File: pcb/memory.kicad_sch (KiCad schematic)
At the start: 0 parts

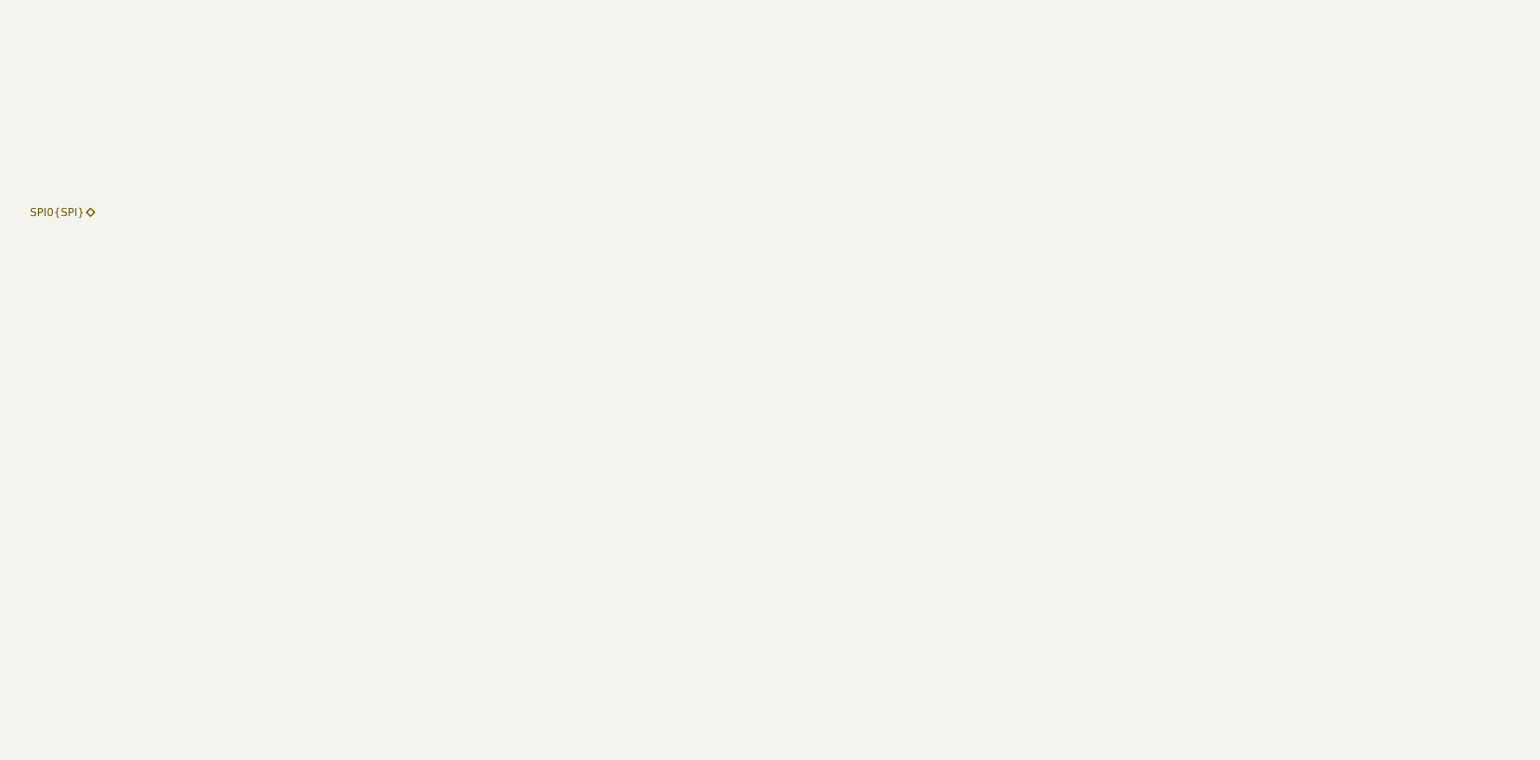
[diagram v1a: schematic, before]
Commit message: current sense hierarchy definition
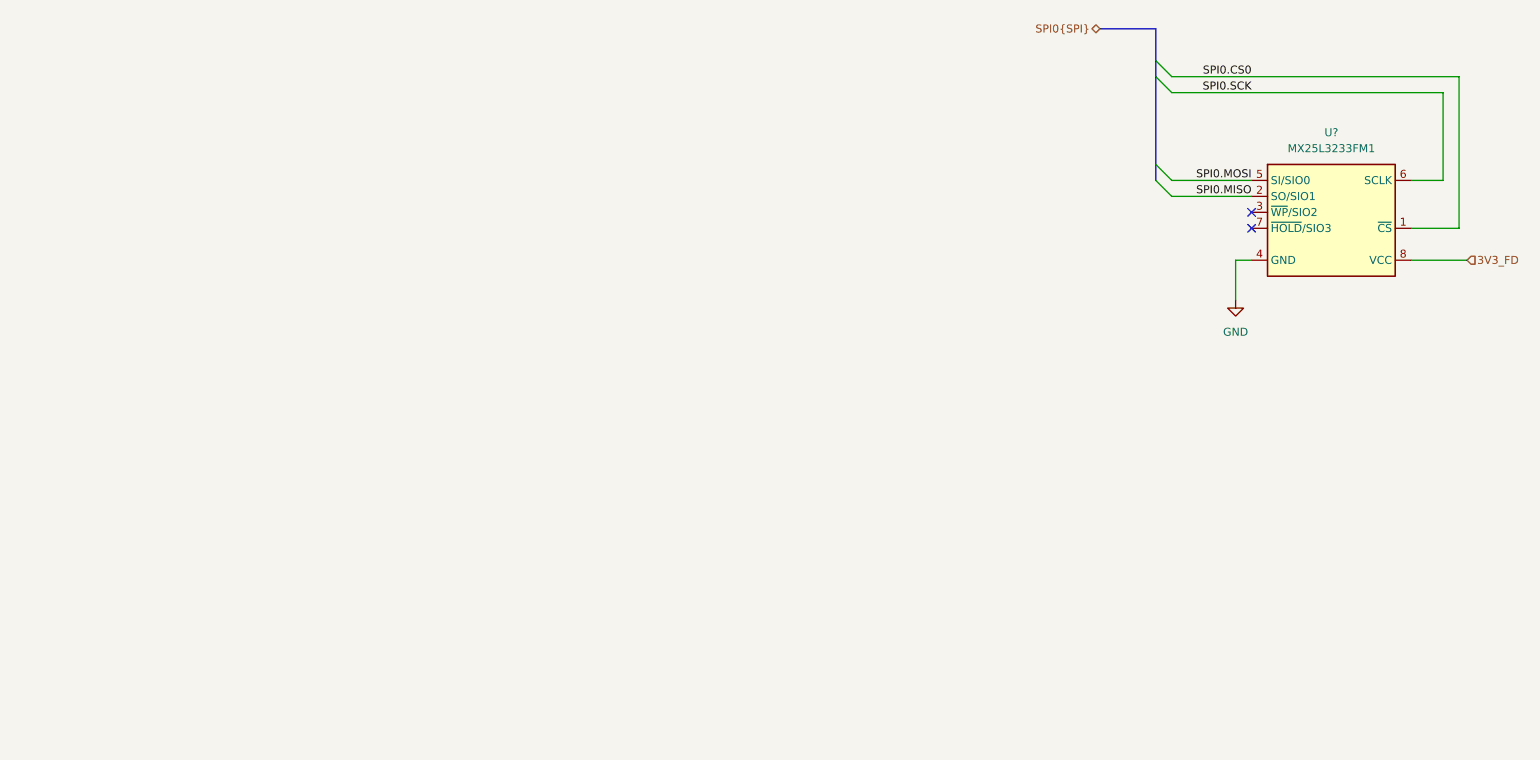
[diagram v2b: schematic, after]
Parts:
- added U?: MX25L3233FM1, Package_SO:JEITA_SOIC-8_3.9x4.9mm_P1.27mm, symbol Memory_Flash:MX25L3233FM1
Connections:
- new net 3V3_FD: U?.8 (VCC)
- new net GND: U?.4 (GND)
- new net SPI0.CS0: U?.1 (~{CS})
- new net SPI0.MISO: U?.2 (SO/SIO1)
- new net SPI0.MOSI: U?.5 (SI/SIO0)
- new net SPI0.SCK: U?.6 (SCLK)
- no-connect marks 0 -> 2

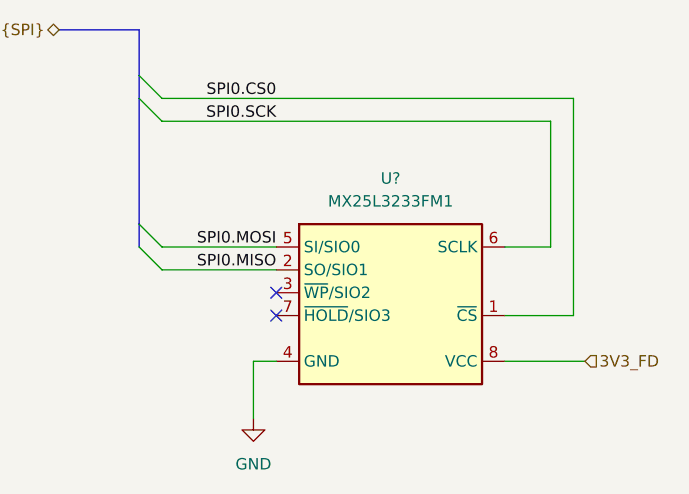
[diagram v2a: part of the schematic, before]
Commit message: changed spi flash to wson
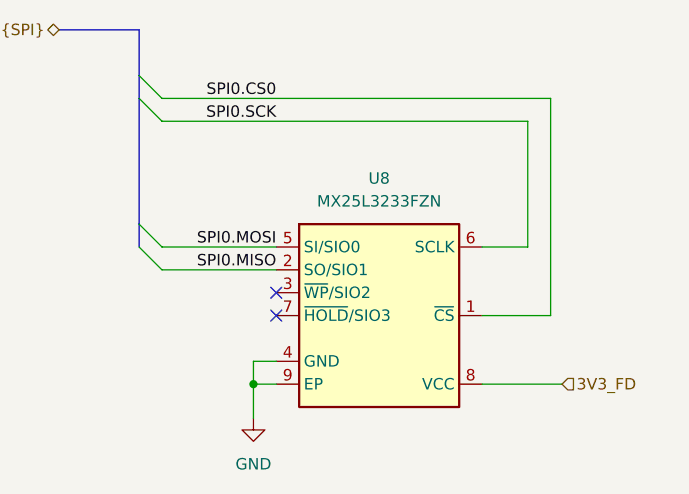
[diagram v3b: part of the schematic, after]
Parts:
- removed U?: MX25L3233FM1, Package_SO:JEITA_SOIC-8_3.9x4.9mm_P1.27mm, symbol Memory_Flash:MX25L3233FM1
- added U8: MX25L3233FZN, Package_SON:WSON-8-1EP_6x5mm_P1.27mm_EP3.4x4mm, symbol Memory_Flash:MX25L3233FZN
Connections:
- net 3V3_FD: now also U8.8 (VCC)
- net GND: now also U8.4 (GND), U8.9 (EP)
- net SPI0.CS0: now also U8.1 (~{CS})
- net SPI0.MISO: now also U8.2 (SO/SIO1)
- net SPI0.MOSI: now also U8.5 (SI/SIO0)
- net SPI0.SCK: now also U8.6 (SCLK)
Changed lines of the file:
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@@
 		(company "Andre S Winkel")
+	)
+	(junction
+		(at 234.95 66.04)
+		(diameter 0)
+		(color 0 0 0 0)
 	)
 	(no_connect
@@
 	(wire
 		(pts
-			(xy 262.89 50.8) (xy 267.97 50.8)
+			(xy 260.35 50.8) (xy 265.43 50.8)
 		)
 		(stroke
@@
 	(wire
 		(pts
-			(xy 270.51 34.29) (xy 270.51 58.42)
+			(xy 267.97 34.29) (xy 267.97 58.42)
 		)
 		(stroke
@@
 	(wire
 		(pts
-			(xy 267.97 36.83) (xy 267.97 50.8)
-		)
-		(stroke
-			(width 0)
-			(type default)
-		)
-	)
-	(wire
-		(pts
-			(xy 262.89 63.5) (xy 271.78 63.5)
-		)
-		(stroke
-			(width 0)
-			(type default)
-		)
-	)
-	(wire
-		(pts
-			(xy 224.79 36.83) (xy 267.97 36.83)
-		)
-		(stroke
-			(width 0)
-			(type default)
-		)
-	)
-	(wire
-		(pts
-			(xy 234.95 63.5) (xy 234.95 69.85)
-		)
-		(stroke
-			(width 0)
-			(type default)
-		)
-	)
-	(wire
-		(pts
-			(xy 262.89 58.42) (xy 270.51 58.42)
+			(xy 265.43 36.83) (xy 265.43 50.8)
+		)
+		(stroke
+			(width 0)
+			(type default)
+		)
+	)
+	(wire
+		(pts
+			(xy 260.35 66.04) (xy 269.24 66.04)
+		)
+		(stroke
+			(width 0)
+			(type default)
+		)
+	)
+	(wire
+		(pts
+			(xy 234.95 66.04) (xy 237.49 66.04)
+		)
+		(stroke
+			(width 0)
+			(type default)
+		)
+	)
+	(wire
+		(pts
+			(xy 224.79 36.83) (xy 265.43 36.83)
+		)
+		(stroke
+			(width 0)
+			(type default)
+		)
+	)
+	(wire
+		(pts
+			(xy 234.95 63.5) (xy 234.95 66.04)
+		)
+		(stroke
+			(width 0)
+			(type default)
+		)
+	)
+	(wire
+		(pts
+			(xy 260.35 58.42) (xy 267.97 58.42)
 		)
 		(stroke
@@
 	(wire
 		(pts
-			(xy 224.79 34.29) (xy 270.51 34.29)
+			(xy 234.95 66.04) (xy 234.95 69.85)
+		)
+		(stroke
+			(width 0)
+			(type default)
+		)
+	)
+	(wire
+		(pts
+			(xy 224.79 34.29) (xy 267.97 34.29)
 		)
 		(stroke
@@
 	(hierarchical_label "3V3_FD"
 		(shape input)
-		(at 271.78 63.5 0)
+		(at 269.24 66.04 0)
 		(effects
 			(font
@@
 	)
 	(symbol
-		(lib_id "Memory_Flash:MX25L3233FM1")
-		(at 250.19 57.15 0)
+		(lib_id "Memory_Flash:MX25L3233FZN")
+		(at 248.92 58.42 0)
 		(unit 1)
 		(exclude_from_sim no)
@@
 		(on_board yes)
 		(dnp no)
-		(property "Reference" "U?"
-			(at 250.19 43.18 0)
-			(effects
-				(font
-					(size 1.27 1.27)
-				)
-			)
-		)
-		(property "Value" "MX25L3233FM1"
-			(at 250.19 45.72 0)
-			(effects
-				(font
-					(size 1.27 1.27)
-				)
-			)
-		)
-		(property "Footprint" "Package_SO:JEITA_SOIC-8_3.9x4.9mm_P1.27mm"
-			(at 250.19 72.39 0)
+		(fields_autoplaced yes)
+		(property "Reference" "U8"
+			(at 248.92 43.18 0)
+			(effects
+				(font
+					(size 1.27 1.27)
+				)
+			)
+		)
+		(property "Value" "MX25L3233FZN"
+			(at 248.92 45.72 0)
+			(effects
+				(font
+					(size 1.27 1.27)
+				)
+			)
+		)
+		(property "Footprint" "Package_SON:WSON-8-1EP_6x5mm_P1.27mm_EP3.4x4mm"
+			(at 248.92 73.66 0)
 			(effects
 				(font
@@
 		)
 		(property "Datasheet" "https://www.macronix.com/Lists/Datasheet/Attachments/8377/MX25L3233F,%203V,%2032Mb,%20v1.1.pdf"
-			(at 250.19 74.676 0)
+			(at 248.92 75.946 0)
 			(effects
 				(font
@@
 			)
 		)
-		(property "Description" "32-Mbit, 3V (2.65V-3.6V) SPI Serial Flash Memory, JEITA SOIC-8 (SOP-8)"
-			(at 247.65 69.85 0)
+		(property "Description" "32-Mbit, 3V (2.65V-3.6V) SPI Serial Flash Memory, WSON-8"
+			(at 247.65 58.42 0)
 			(effects
 				(font
@@
 		)
 		(property "Name" ""
-			(at 250.19 57.15 0)
+			(at 248.92 58.42 0)
 			(effects
 				(font
@@
 			)
 		)
+		(pin "4"
+		)
+		(pin "8"
+		)
+		(pin "7"
+		)
+		(pin "3"
+		)
+		(pin "2"
+		)
+		(pin "5"
+		)
+		(pin "6"
+		)
 		(pin "1"
 		)
-		(pin "6"
-		)
-		(pin "5"
-		)
-		(pin "2"
-		)
-		(pin "3"
-		)
-		(pin "7"
-		)
-		(pin "8"
-		)
-		(pin "4"
+		(pin "9"
 		)
 		(instances
 			(project ""
 				(path "/e63e39d7-6ac0-4ffd-8aa3-1841a4541b55/59d21473-a004-4514-8090-fd93db818925/b633a666-4c3d-4ac9-9e0f-b350177ade0b"
-					(reference "U?")
+					(reference "U8")
 					(unit 1)
 				)

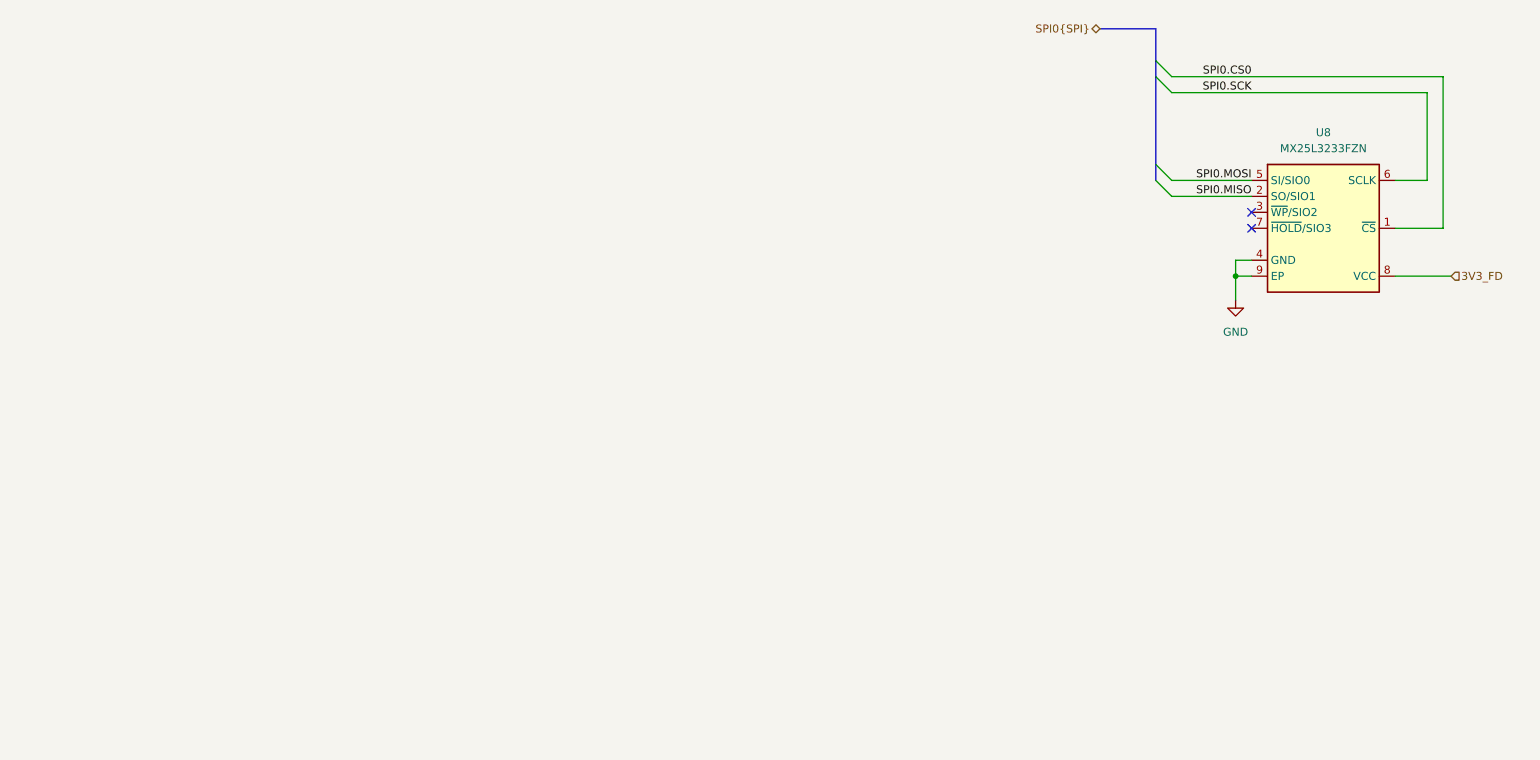
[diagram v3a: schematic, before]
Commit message: added dram, defined pcie sideband sigs.
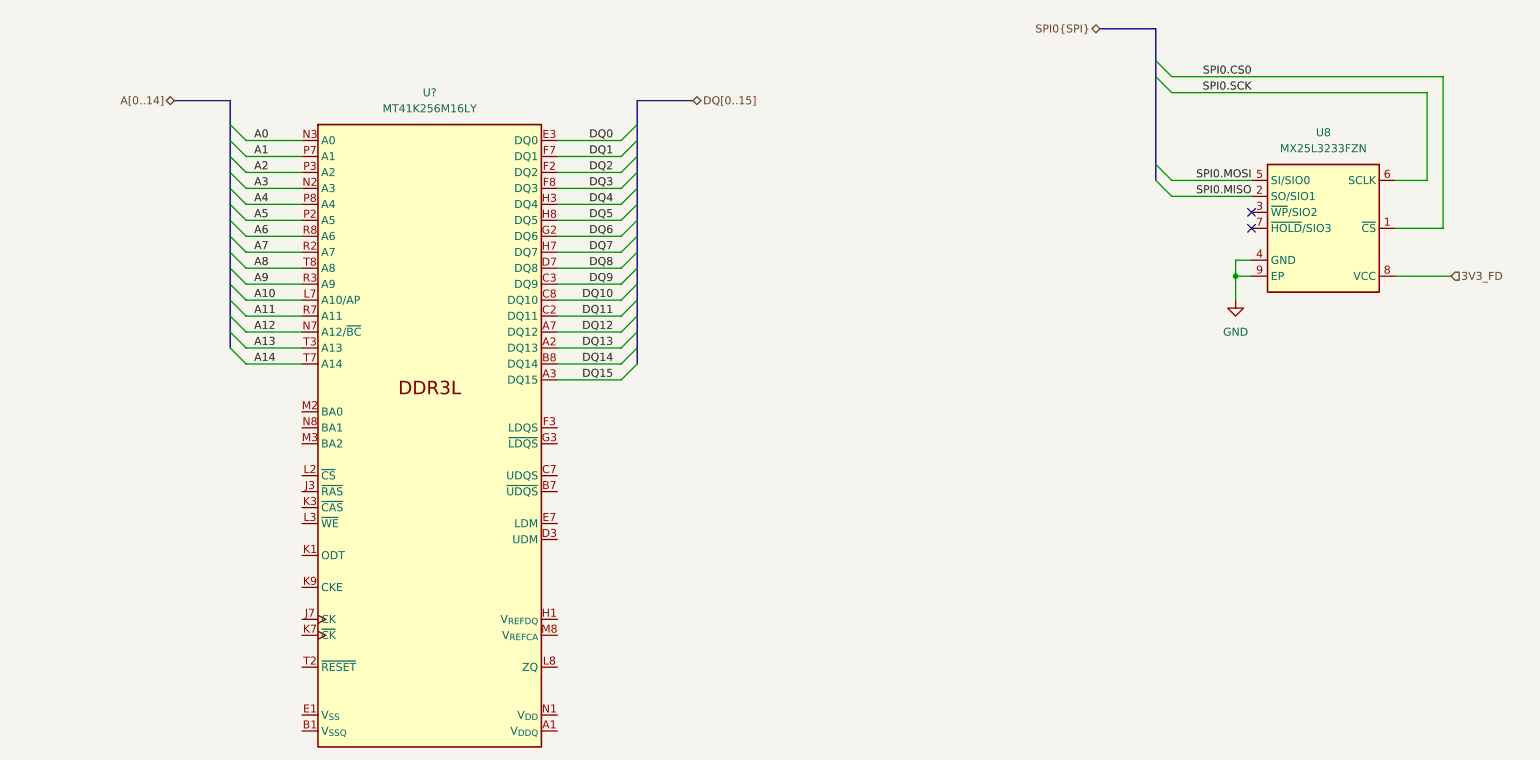
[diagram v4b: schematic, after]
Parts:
- added U?: MT41K256M16LY, Package_BGA:Micron_FBGA-96_7.5x13.5mm_Layout9x16_P0.8mm, symbol Memory_RAM:MT41K256M16LY
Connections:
- new net: U?.A8 (V_{DDQ}), U?.C1 (V_{DDQ}), U?.C9 (V_{DDQ}), U?.D2 (V_{DDQ}), U?.E9 (V_{DDQ}), U?.F1 (V_{DDQ}), U?.H2 (V_{DDQ}), U?.H9 (V_{DDQ})
- new net: U?.A9 (V_{SS}), U?.B3 (V_{SS}), U?.G8 (V_{SS}), U?.J2 (V_{SS}), U?.J8 (V_{SS}), U?.M1 (V_{SS}), U?.M9 (V_{SS}), U?.P1 (V_{SS}), U?.P9 (V_{SS}), U?.T1 (V_{SS}), U?.T9 (V_{SS})
- new net: U?.B2 (V_{DD}), U?.D9 (V_{DD}), U?.G7 (V_{DD}), U?.K2 (V_{DD}), U?.K8 (V_{DD}), U?.N9 (V_{DD}), U?.R1 (V_{DD}), U?.R9 (V_{DD})
- new net: U?.B9 (V_{SSQ}), U?.D1 (V_{SSQ}), U?.D8 (V_{SSQ}), U?.E2 (V_{SSQ}), U?.E8 (V_{SSQ}), U?.F9 (V_{SSQ}), U?.G1 (V_{SSQ}), U?.G9 (V_{SSQ})
- new net A0: U?.N3 (A0)
- new net A1: U?.P7 (A1)
- new net A10: U?.L7 (A10/AP)
- new net A11: U?.R7 (A11)
- new net A12: U?.N7 (A12/~{BC})
- new net A13: U?.T3 (A13)
- new net A14: U?.T7 (A14)
- new net A2: U?.P3 (A2)
- new net A3: U?.N2 (A3)
- new net A4: U?.P8 (A4)
- new net A5: U?.P2 (A5)
- new net A6: U?.R8 (A6)
- new net A7: U?.R2 (A7)
- new net A8: U?.T8 (A8)
- new net A9: U?.R3 (A9)
- new net DQ0: U?.E3 (DQ0)
- new net DQ1: U?.F7 (DQ1)
- new net DQ10: U?.C8 (DQ10)
- new net DQ11: U?.C2 (DQ11)
- new net DQ12: U?.A7 (DQ12)
- new net DQ13: U?.A2 (DQ13)
- new net DQ14: U?.B8 (DQ14)
- new net DQ15: U?.A3 (DQ15)
- new net DQ2: U?.F2 (DQ2)
- new net DQ3: U?.F8 (DQ3)
- new net DQ4: U?.H3 (DQ4)
- new net DQ5: U?.H8 (DQ5)
- new net DQ6: U?.G2 (DQ6)
- new net DQ7: U?.H7 (DQ7)
- new net DQ8: U?.D7 (DQ8)
- new net DQ9: U?.C3 (DQ9)

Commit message: ddr3
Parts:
- added U?: TCR2EE135, Package_TO_SOT_SMD:SOT-553, symbol Regulator_Linear:TCR2EE135
- gave numbers to parts that had none: 1
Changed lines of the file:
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@@
+	)
+	(symbol
+		(lib_id "Regulator_Linear:TCR2EE135")
+		(at 165.1 100.33 0)
+		(unit 1)
+		(exclude_from_sim no)
+		(in_bom yes)
+		(on_board yes)
+		(dnp no)
+		(fields_autoplaced yes)
+		(property "Reference" "U?"
+			(at 165.1 90.17 0)
+			(effects
+				(font
+					(size 1.27 1.27)
+				)
+			)
+		)
+		(property "Value" "TCR2EE135"
+			(at 165.1 92.71 0)
+			(effects
+				(font
+					(size 1.27 1.27)
+				)
+			)
+		)
+		(property "Footprint" "Package_TO_SOT_SMD:SOT-553"
+			(at 165.1 110.49 0)
+			(effects
+				(font
+					(size 1.27 1.27)
+				)
+				(hide yes)
+			)
+		)
+		(property "Datasheet" "https://toshiba.semicon-storage.com/info/docget.jsp?did=13794&prodName=TCR2EF45"
+			(at 158.75 93.98 0)
+			(effects
+				(font
+					(size 1.27 1.27)
+				)
+				(hide yes)
+			)
+		)
+		(property "Description" "200mA Low-dropout Voltage Regulator, Vout 1.35V, Vin up to 5.5V, SOT-553"
+			(at 165.1 100.33 0)
+			(effects
+				(font
+					(size 1.27 1.27)
+				)
+				(hide yes)
+			)
+		)
+		(property "Name" ""
+			(at 165.1 100.33 0)
+			(effects
+				(font
+					(size 1.27 1.27)
+				)
+				(hide yes)
+			)
+		)
+		(pin "5"
+		)
+		(pin "2"
+		)
+		(pin "1"
+		)
+		(pin "3"
+		)
+		(pin "4"
+		)
+		(instances
+			(project ""
+				(path "/e63e39d7-6ac0-4ffd-8aa3-1841a4541b55/59d21473-a004-4514-8090-fd93db818925/b633a666-4c3d-4ac9-9e0f-b350177ade0b"
+					(reference "U?")
+					(unit 1)
+				)
+			)
+		)
 	)
 	(symbol
@@
 		(dnp no)
 		(fields_autoplaced yes)
-		(property "Reference" "U?"
+		(property "Reference" "U7"
 			(at 106.68 36.83 0)
 			(effects
@@
 			(project ""
 				(path "/e63e39d7-6ac0-4ffd-8aa3-1841a4541b55/59d21473-a004-4514-8090-fd93db818925/b633a666-4c3d-4ac9-9e0f-b350177ade0b"
-					(reference "U?")
+					(reference "U7")
 					(unit 1)
 				)

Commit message: saved libraries to project
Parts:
- U7: symbol Memory_RAM:MT41K256M16LY -> library:MT41K256M16LY
- U8: symbol Memory_Flash:MX25L3233FZN -> library:MX25L3233FZN
- U?: symbol Regulator_Linear:TCR2EE135 -> library:TCR2EE135
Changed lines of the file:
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@@
 	)
 	(symbol
-		(lib_id "Memory_Flash:MX25L3233FZN")
+		(lib_id "library:MX25L3233FZN")
 		(at 248.92 58.42 0)
 		(unit 1)
@@
 	)
 	(symbol
-		(lib_id "Regulator_Linear:TCR2EE135")
+		(lib_id "library:TCR2EE135")
 		(at 165.1 100.33 0)
 		(unit 1)
@@
 	)
 	(symbol
-		(lib_id "Memory_RAM:MT41K256M16LY")
+		(lib_id "library:MT41K256M16LY")
 		(at 106.68 85.09 0)
 		(unit 1)
@@
 	)
 	(symbol
-		(lib_id "power:GND")
+		(lib_id "library:GND")
 		(at 234.95 69.85 0)
 		(unit 1)
